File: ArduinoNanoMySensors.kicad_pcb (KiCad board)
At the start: 2 copper layers, 16 parts, among them P1 CONN_02X15, P2 CONN_02X15, T1 DS18b20 DS18B20

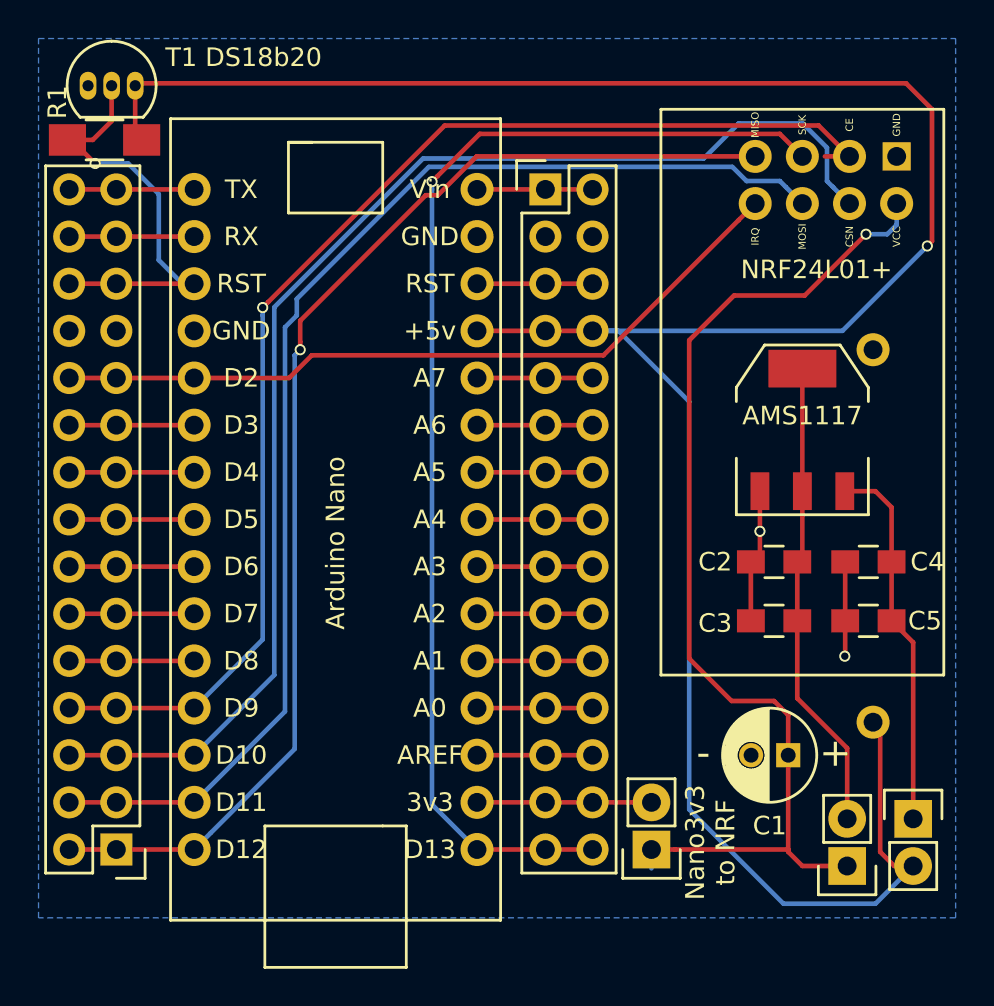
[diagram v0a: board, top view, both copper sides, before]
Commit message: Made v0.2 with the following changes:
- plus en min op batterij x
-batterijpins dikker x
-nanopins dikker x
-nrf pins dikker x
-polariteit duidelijk bij C1x
- naamgeving componenten x
-polariteit en vakjes voor jumpers x
-optioneel 3v3 van arduino  x
-3v3 direct van batterij naar nrf x
-pins van NRF op juiste pins... x
-uitzoeken voeden van arduino via batterij x
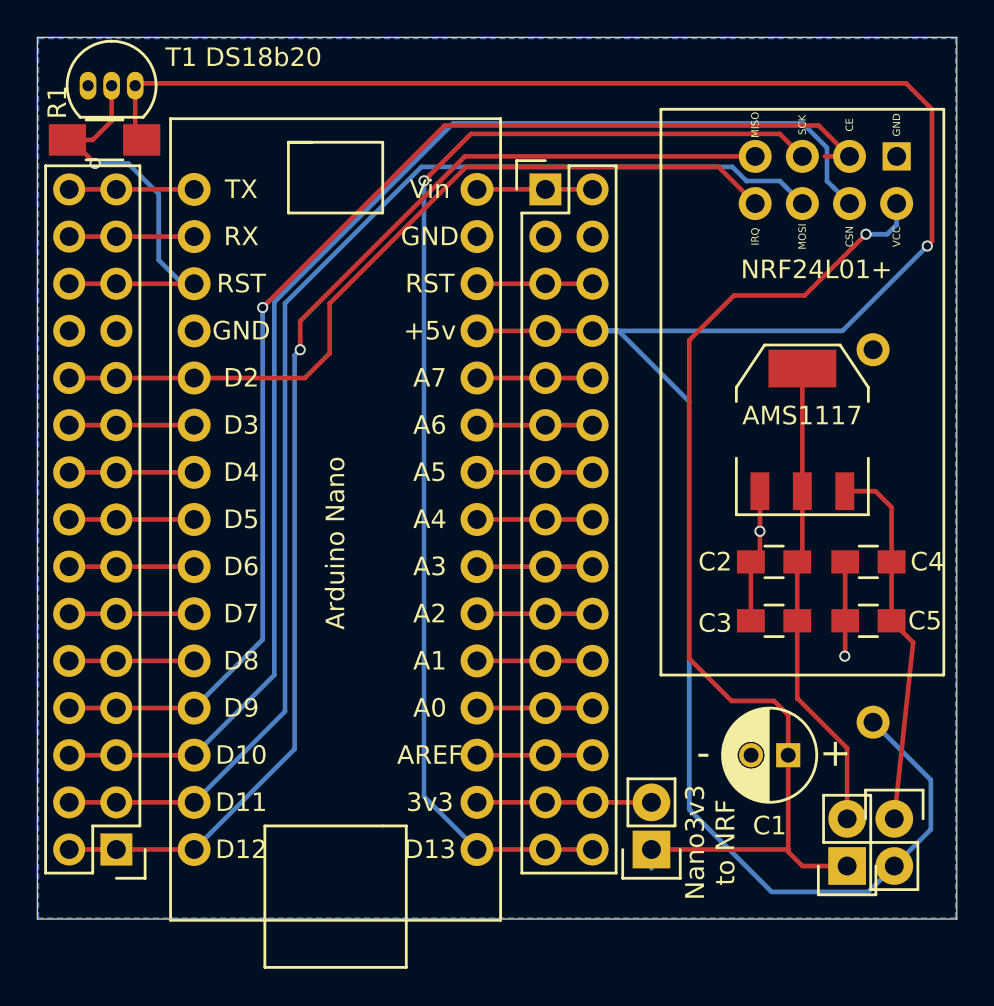
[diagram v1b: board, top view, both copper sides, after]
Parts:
- moved JP2 1.02 mm to (178.7, 129.2)
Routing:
- net Net-(P1-Pad21): track 40.8 -> 44.1 mm
- net Net-(P2-Pad29): track 64.7 -> 65.4 mm
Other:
- board outline added: 49.5 x 47.5 mm
- board text added: "MySensors Basic-board V0.2 By Marco van Noord see: https://git.io/vKyrr"
- board text added: "See docs before using jumpers!"
- board text removed: "MySensors Basic-board V0.1 By Marco van Noord"
